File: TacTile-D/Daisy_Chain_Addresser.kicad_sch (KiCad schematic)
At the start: 6 parts, among them U1 74LS04, U16 74LS74, U2 4011, U6 74HC08, U7 74LS74, U9 74HC4051

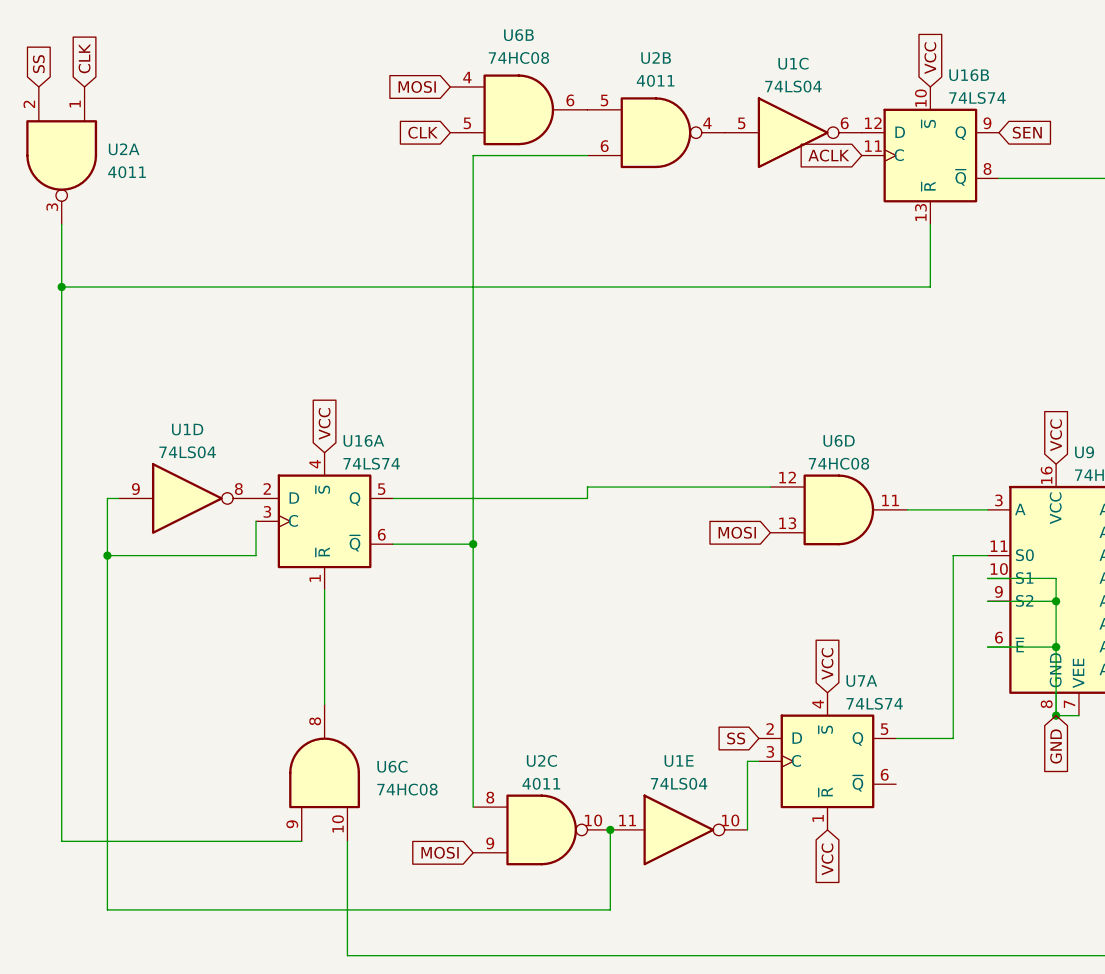
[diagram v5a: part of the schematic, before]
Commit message: Fixed counter clocking delay on D board
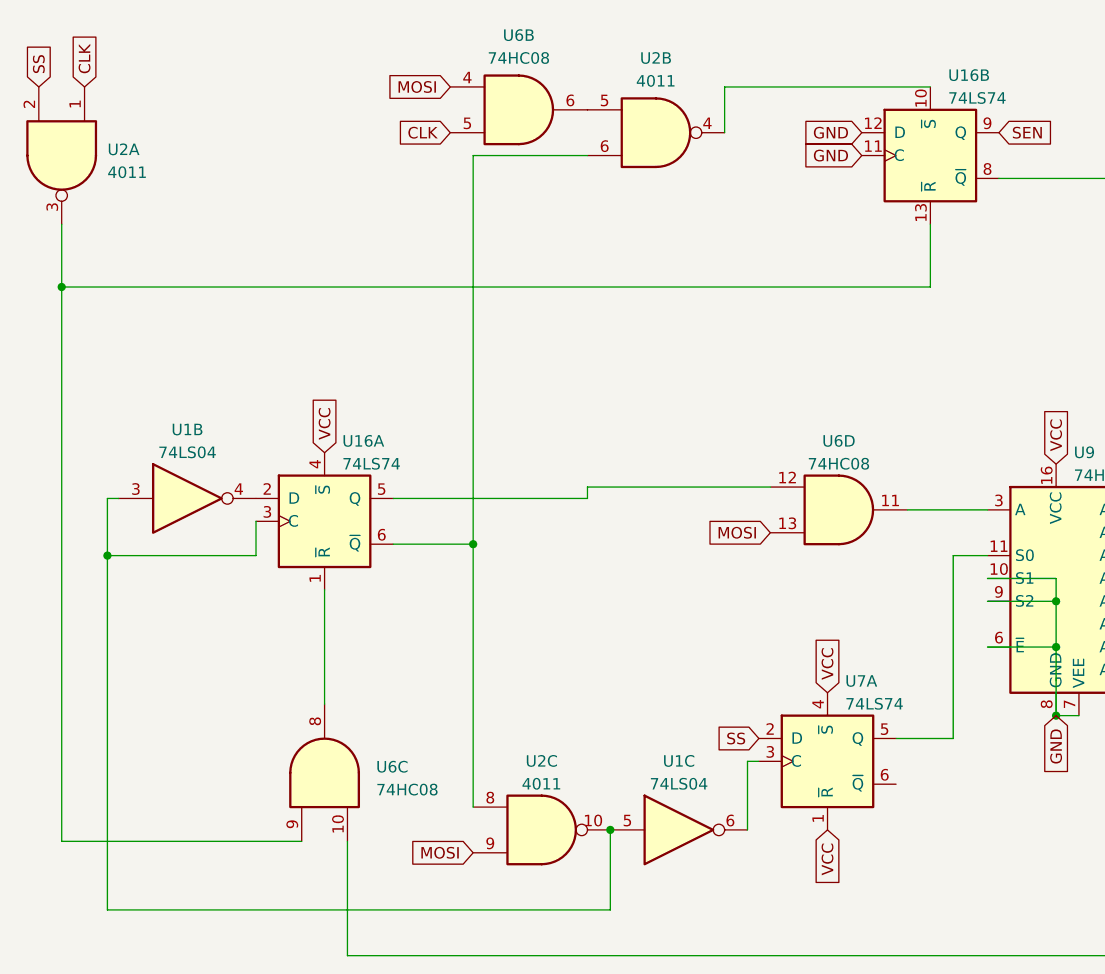
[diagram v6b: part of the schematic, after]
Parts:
- removed unit 5 of U1
- removed unit 4 of U1
- added unit 2 of U1
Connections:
- net ACLK is gone; now on net GND: U16.11 (C)
- net GND: now also U16.12 (D)
- net VCC: no longer U16.10 (~{S})
- net at U16.2 (D): now also U1.4
- net at U16.3 (C), U2.10: now also U1.5, U1.3
- net at U1.6: now also U7.3 (C); no longer U16.12 (D)
- net at U2.4: now also U16.10 (~{S}); no longer U1.5
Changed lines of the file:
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@@
 (kicad_sch (version 20230121) (generator eeschema)
   (paper "A4")
+  (junction (at 88.9 104.14) (diameter 0) (color 0 0 0 0)
+  )
   (junction (at 33.02 73.66) (diameter 0) (color 0 0 0 0)
   )
   (junction (at 138.43 78.74) (diameter 0) (color 0 0 0 0)
   )
-  (junction (at 88.9 104.14) (diameter 0) (color 0 0 0 0)
-  )
   (junction (at 138.43 83.82) (diameter 0) (color 0 0 0 0)
   )
@@
     (stroke (width 0) (type default))
   )
+  (wire (pts (xy 101.6 21.59) (xy 124.46 21.59))
+    (stroke (width 0) (type default))
+  )
   (wire (pts (xy 104.14 96.52) (xy 105.41 96.52))
     (stroke (width 0) (type default))
@@
     (stroke (width 0) (type default))
   )
+  (wire (pts (xy 101.6 26.67) (xy 101.6 21.59))
+    (stroke (width 0) (type default))
+  )
   (wire (pts (xy 73.66 72.39) (xy 73.66 29.21))
     (stroke (width 0) (type default))
@@
     (stroke (width 0) (type default))
   )
-  (global_label "VCC" (shape input) (at 124.46 21.59 90) (fields_autoplaced)
-    (effects (font (size 1.27 1.27)) (justify left))
-    (property "Intersheetrefs" "${INTERSHEET_REFS}" (at 124.46 15.0556 90)
-      (effects (font (size 1.27 1.27)) (justify left) hide)
-    )
-  )
   (global_label "CLK" (shape input) (at 30.48 21.59 90) (fields_autoplaced)
     (effects (font (size 1.27 1.27)) (justify left))
@@
     )
   )
-  (global_label "ACLK" (shape input) (at 116.84 29.21 180) (fields_autoplaced)
-    (effects (font (size 1.27 1.27)) (justify right))
-    (property "Intersheetrefs" "${INTERSHEET_REFS}" (at 109.2775 29.21 0)
-      (effects (font (size 1.27 1.27)) (justify right) hide)
-    )
-  )
   (global_label "VCC" (shape input) (at 113.03 88.9 90) (fields_autoplaced)
     (effects (font (size 1.27 1.27)) (justify left))
@@
     )
   )
+  (global_label "GND" (shape input) (at 116.84 29.21 180) (fields_autoplaced)
+    (effects (font (size 1.27 1.27)) (justify right))
+    (property "Intersheetrefs" "${INTERSHEET_REFS}" (at 110.0637 29.21 0)
+      (effects (font (size 1.27 1.27)) (justify right) hide)
+    )
+  )
   (global_label "VCC" (shape input) (at 250.825 72.39 180) (fields_autoplaced)
     (effects (font (size 1.27 1.27)) (justify right))
@@
     )
   )
+  (global_label "GND" (shape input) (at 116.84 26.67 180) (fields_autoplaced)
+    (effects (font (size 1.27 1.27)) (justify right))
+    (property "Intersheetrefs" "${INTERSHEET_REFS}" (at 110.0637 26.67 0)
+      (effects (font (size 1.27 1.27)) (justify right) hide)
+    )
+  )
   (global_label "VCC" (shape input) (at 257.81 24.13 180) (fields_autoplaced)
     (effects (font (size 1.27 1.27)) (justify right))
@@
         (path "/99b9cae1-6ece-4124-abcb-60ec0df49dce/db500e62-b4b7-46ca-b547-61dad2cea336"
           (reference "U6") (unit 2)
+        )
+      )
+    )
+  )
+  (symbol (lib_id "74xx:74LS04") (at 41.91 67.31 0) (unit 2)
+    (in_bom yes) (on_board yes) (dnp no) (fields_autoplaced)
+    (property "Reference" "U1" (at 41.91 59.69 0)
+      (effects (font (size 1.27 1.27)))
+    )
+    (property "Value" "74LS04" (at 41.91 62.23 0)
+      (effects (font (size 1.27 1.27)))
+    )
+    (property "Footprint" "" (at 41.91 67.31 0)
+      (effects (font (size 1.27 1.27)) hide)
+    )
+    (property "Datasheet" "http://www.ti.com/lit/gpn/sn74LS04" (at 41.91 67.31 0)
+      (effects (font (size 1.27 1.27)) hide)
+    )
+    (pin "1")
+    (pin "2")
+    (pin "3")
+    (pin "4")
+    (pin "5")
+    (pin "6")
+    (pin "8")
+    (pin "9")
+    (pin "10")
+    (pin "11")
+    (pin "12")
+    (pin "13")
+    (pin "14")
+    (pin "7")
+    (instances
+      (project "TacTile-D"
+        (path "/99b9cae1-6ece-4124-abcb-60ec0df49dce/db500e62-b4b7-46ca-b547-61dad2cea336"
+          (reference "U1") (unit 2)
         )
       )
@@
     )
   )
+  (symbol (lib_id "74xx:74LS04") (at 96.52 104.14 0) (unit 3)
+    (in_bom yes) (on_board yes) (dnp no) (fields_autoplaced)
+    (property "Reference" "U1" (at 96.52 96.52 0)
+      (effects (font (size 1.27 1.27)))
+    )
+    (property "Value" "74LS04" (at 96.52 99.06 0)
+      (effects (font (size 1.27 1.27)))
+    )
+    (property "Footprint" "" (at 96.52 104.14 0)
+      (effects (font (size 1.27 1.27)) hide)
+    )
+    (property "Datasheet" "http://www.ti.com/lit/gpn/sn74LS04" (at 96.52 104.14 0)
+      (effects (font (size 1.27 1.27)) hide)
+    )
+    (pin "1")
+    (pin "2")
+    (pin "3")
+    (pin "4")
+    (pin "5")
+    (pin "6")
+    (pin "8")
+    (pin "9")
+    (pin "10")
+    (pin "11")
+    (pin "12")
+    (pin "13")
+    (pin "14")
+    (pin "7")
+    (instances
+      (project "TacTile-D"
+        (path "/99b9cae1-6ece-4124-abcb-60ec0df49dce/db500e62-b4b7-46ca-b547-61dad2cea336"
+          (reference "U1") (unit 3)
+        )
+      )
+    )
+  )
   (symbol (lib_id "74xx:74HC4051") (at 138.43 76.2 0) (unit 1)
     (in_bom yes) (on_board yes) (dnp no) (fields_autoplaced)
@@
         (path "/99b9cae1-6ece-4124-abcb-60ec0df49dce/db500e62-b4b7-46ca-b547-61dad2cea336"
           (reference "U7") (unit 3)
-        )
-      )
-    )
-  )
-  (symbol (lib_id "74xx:74LS04") (at 96.52 104.14 0) (unit 5)
-    (in_bom yes) (on_board yes) (dnp no) (fields_autoplaced)
-    (property "Reference" "U1" (at 96.52 96.52 0)
-      (effects (font (size 1.27 1.27)))
-    )
-    (property "Value" "74LS04" (at 96.52 99.06 0)
-      (effects (font (size 1.27 1.27)))
-    )
-    (property "Footprint" "Package_DIP:DIP-14_W7.62mm" (at 96.52 104.14 0)
-      (effects (font (size 1.27 1.27)) hide)
-    )
-    (property "Datasheet" "http://www.ti.com/lit/gpn/sn74LS04" (at 96.52 104.14 0)
-      (effects (font (size 1.27 1.27)) hide)
-    )
-    (pin "1")
-    (pin "2")
-    (pin "3")
-    (pin "4")
-    (pin "5")
-    (pin "6")
-    (pin "8")
-    (pin "9")
-    (pin "10")
-    (pin "11")
-    (pin "12")
-    (pin "13")
-    (pin "14")
-    (pin "7")
-    (instances
-      (project "TacTile-D"
-        (path "/99b9cae1-6ece-4124-abcb-60ec0df49dce/db500e62-b4b7-46ca-b547-61dad2cea336"
-          (reference "U1") (unit 5)
-        )
-        (path "/99b9cae1-6ece-4124-abcb-60ec0df49dce"
-          (reference "U1") (unit 5)
         )
       )
@@
     )
   )
-  (symbol (lib_id "74xx:74LS04") (at 109.22 26.67 0) (unit 3)
-    (in_bom yes) (on_board yes) (dnp no) (fields_autoplaced)
-    (property "Reference" "U1" (at 109.22 19.05 0)
-      (effects (font (size 1.27 1.27)))
-    )
-    (property "Value" "74LS04" (at 109.22 21.59 0)
-      (effects (font (size 1.27 1.27)))
-    )
-    (property "Footprint" "" (at 109.22 26.67 0)
-      (effects (font (size 1.27 1.27)) hide)
-    )
-    (property "Datasheet" "http://www.ti.com/lit/gpn/sn74LS04" (at 109.22 26.67 0)
-      (effects (font (size 1.27 1.27)) hide)
-    )
-    (pin "1")
-    (pin "2")
-    (pin "3")
-    (pin "4")
-    (pin "5")
-    (pin "6")
-    (pin "8")
-    (pin "9")
-    (pin "10")
-    (pin "11")
-    (pin "12")
-    (pin "13")
-    (pin "14")
-    (pin "7")
-    (instances
-      (project "TacTile-D"
-        (path "/99b9cae1-6ece-4124-abcb-60ec0df49dce/db500e62-b4b7-46ca-b547-61dad2cea336"
-          (reference "U1") (unit 3)
-        )
-      )
-    )
-  )
   (symbol (lib_id "4xxx:4011") (at 93.98 26.67 0) (unit 2)
     (in_bom yes) (on_board yes) (dnp no) (fields_autoplaced)
@@
         )
       )
-    )
-  )
-  (symbol (lib_id "74xx:74LS04") (at 41.91 67.31 0) (unit 4)
-    (in_bom yes) (on_board yes) (dnp no) (fields_autoplaced)
-    (property "Reference" "U1" (at 41.91 59.69 0)
-      (effects (font (size 1.27 1.27)))
-    )
-    (property "Value" "74LS04" (at 41.91 62.23 0)
-      (effects (font (size 1.27 1.27)))
-    )
-    (property "Footprint" "Package_DIP:DIP-14_W7.62mm" (at 41.91 67.31 0)
-      (effects (font (size 1.27 1.27)) hide)
-    )
-    (property "Datasheet" "http://www.ti.com/lit/gpn/sn74LS04" (at 41.91 67.31 0)
-      (effects (font (size 1.27 1.27)) hide)
-    )
-    (pin "1")
-    (pin "2")
-    (pin "3")
-    (pin "4")
-    (pin "5")
-    (pin "6")
-    (pin "8")
-    (pin "9")
-    (pin "10")
-    (pin "11")
-    (pin "12")
-    (pin "13")
-    (pin "14")
-    (pin "7")
-    (instances
-      (project "TacTile-D"
-        (path "/99b9cae1-6ece-4124-abcb-60ec0df49dce/db500e62-b4b7-46ca-b547-61dad2cea336"
-          (reference "U1") (unit 4)
-        )
-        (path "/99b9cae1-6ece-4124-abcb-60ec0df49dce"
-          (reference "U1") (unit 4)
-        )
-      )
